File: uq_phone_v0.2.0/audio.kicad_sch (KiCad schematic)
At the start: 31 parts, among them J1 PJ-605, U13 TS3A5018RSVR, U14 NAU88C22YG, U9 AZV5001RA4-7

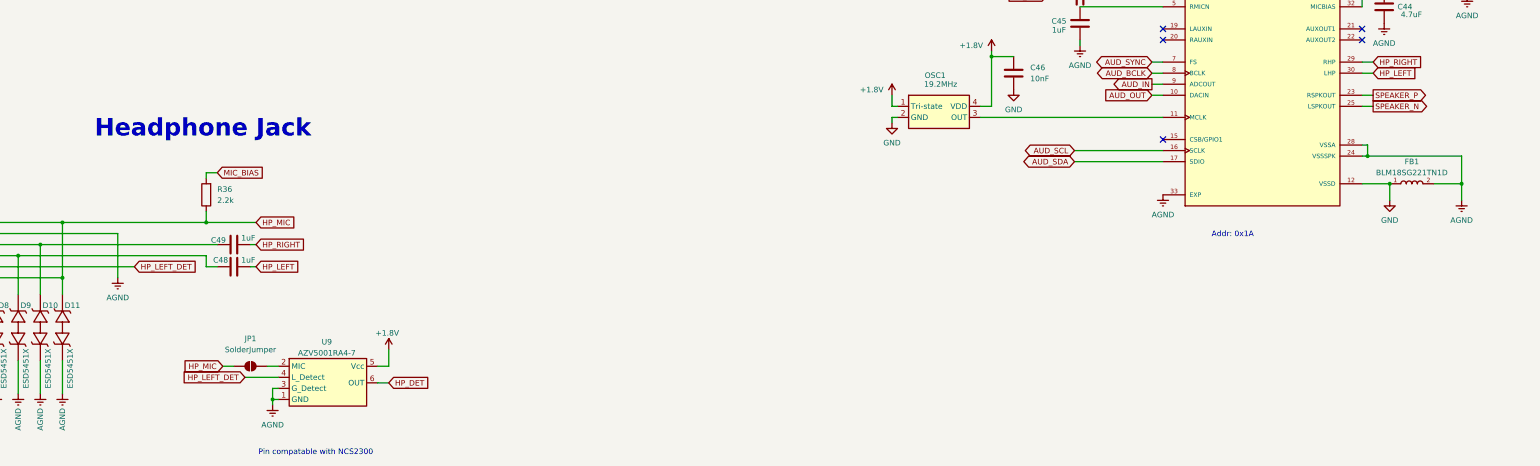
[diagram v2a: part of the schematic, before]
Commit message: Fixed display pinout
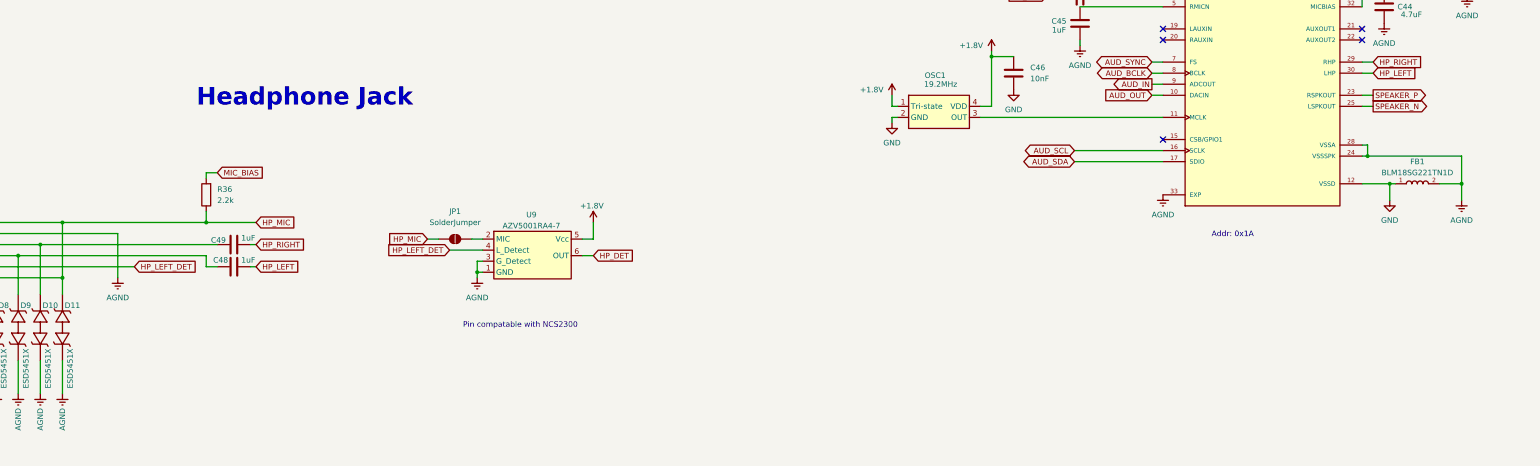
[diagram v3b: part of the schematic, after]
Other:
- moved on the sheet: FB1, JP1, U9
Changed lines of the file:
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@@
 	(text "Pin compatable with NCS2300"
 		(exclude_from_sim no)
-		(at 112.776 271.272 0)
+		(at 159.766 242.062 0)
 		(effects
 			(font
@@
 	(text "Headphone Jack"
 		(exclude_from_sim no)
-		(at 86.868 196.85 0)
+		(at 110.236 189.738 0)
 		(effects
 			(font
@@
 	)
 	(junction
-		(at 102.87 259.08)
+		(at 149.86 229.87)
 		(diameter 0)
 		(color 0 0 0 0)
@@
 	(wire
 		(pts
-			(xy 91.44 251.46) (xy 93.98 251.46)
+			(xy 138.43 222.25) (xy 140.97 222.25)
 		)
 		(stroke
@@
 	(wire
 		(pts
-			(xy 102.87 256.54) (xy 102.87 259.08)
+			(xy 149.86 227.33) (xy 149.86 229.87)
 		)
 		(stroke
@@
 	(wire
 		(pts
-			(xy 102.87 259.08) (xy 104.14 259.08)
+			(xy 149.86 229.87) (xy 151.13 229.87)
 		)
 		(stroke
@@
 	(wire
 		(pts
-			(xy 375.92 209.55) (xy 369.57 209.55)
+			(xy 375.92 209.55) (xy 370.84 209.55)
 		)
 		(stroke
@@
 	(wire
 		(pts
-			(xy 96.52 254) (xy 104.14 254)
+			(xy 143.51 224.79) (xy 151.13 224.79)
 		)
 		(stroke
@@
 	(wire
 		(pts
-			(xy 101.6 251.46) (xy 104.14 251.46)
+			(xy 148.59 222.25) (xy 151.13 222.25)
 		)
 		(stroke
@@
 	(wire
 		(pts
+			(xy 360.68 209.55) (xy 359.41 209.55)
+		)
+		(stroke
+			(width 0)
+			(type default)
+		)
+	)
+	(wire
+		(pts
 			(xy 378.46 129.54) (xy 378.46 130.81)
 		)
@@
 	(wire
 		(pts
-			(xy 129.54 251.46) (xy 127 251.46)
+			(xy 176.53 222.25) (xy 173.99 222.25)
 		)
 		(stroke
@@
 	(wire
 		(pts
-			(xy 102.87 260.35) (xy 102.87 259.08)
+			(xy 149.86 231.14) (xy 149.86 229.87)
 		)
 		(stroke
@@
 	(wire
 		(pts
-			(xy 129.54 247.65) (xy 129.54 251.46)
+			(xy 176.53 218.44) (xy 176.53 222.25)
 		)
 		(stroke
@@
 	(wire
 		(pts
-			(xy 129.54 255.27) (xy 127 255.27)
+			(xy 176.53 226.06) (xy 173.99 226.06)
 		)
 		(stroke
@@
 	(wire
 		(pts
-			(xy 104.14 256.54) (xy 102.87 256.54)
+			(xy 151.13 227.33) (xy 149.86 227.33)
 		)
 		(stroke
@@
 	(global_label "HP_DET"
 		(shape input)
-		(at 129.54 255.27 0)
+		(at 176.53 226.06 0)
 		(fields_autoplaced yes)
 		(effects
@@
 		)
 		(property "Intersheetrefs" "${INTERSHEET_REFS}"
-			(at 139.4799 255.27 0)
+			(at 186.4699 226.06 0)
 			(effects
 				(font
@@
 	(global_label "HP_LEFT_DET"
 		(shape input)
-		(at 96.52 254 180)
+		(at 143.51 224.79 180)
 		(fields_autoplaced yes)
 		(effects
@@
 		)
 		(property "Intersheetrefs" "${INTERSHEET_REFS}"
-			(at 81.3792 254 0)
+			(at 128.3692 224.79 0)
 			(effects
 				(font
@@
 	(global_label "HP_MIC"
 		(shape input)
-		(at 91.44 251.46 180)
+		(at 138.43 222.25 180)
 		(fields_autoplaced yes)
 		(effects
@@
 		)
 		(property "Intersheetrefs" "${INTERSHEET_REFS}"
-			(at 81.5605 251.46 0)
+			(at 128.5505 222.25 0)
 			(effects
 				(font
@@
 	(symbol
 		(lib_id "Misc:AZV5001")
-		(at 104.14 254 0)
+		(at 151.13 224.79 0)
 		(unit 1)
 		(exclude_from_sim no)
@@
 		(dnp no)
 		(property "Reference" "U9"
-			(at 115.316 245.872 0)
+			(at 162.306 216.662 0)
 			(effects
 				(font
@@
 		)
 		(property "Value" "AZV5001RA4-7"
-			(at 115.316 248.412 0)
+			(at 162.306 219.202 0)
 			(effects
 				(font
@@
 		)
 		(property "Footprint" "custom_footprints:DFN1210P6X_L1.2-W1.0-P0.40-BL"
-			(at 102.87 237.998 0)
+			(at 149.86 208.788 0)
 			(effects
 				(font
@@
 		)
 		(property "Datasheet" "https://www.lcsc.com/product-detail/C5246088.html?s_z=n_AZV5001"
-			(at 102.87 237.998 0)
+			(at 149.86 208.788 0)
 			(effects
 				(font
@@
 		)
 		(property "Description" "Low-Power Headset Detection IC in Miniaturized Package"
-			(at 102.87 237.998 0)
+			(at 149.86 208.788 0)
 			(effects
 				(font
@@
 		)
 		(property "LCSC PN" "C5246088"
-			(at 102.87 237.998 0)
+			(at 149.86 208.788 0)
 			(effects
 				(font
@@
 		)
 		(property "DESCRIPTION" ""
-			(at 104.14 254 0)
+			(at 151.13 224.79 0)
 			(effects
 				(font
@@
 		)
 		(property "LSCS PN" ""
-			(at 104.14 254 0)
+			(at 151.13 224.79 0)
 			(effects
 				(font
@@
 	(symbol
 		(lib_id "power:GNDREF")
-		(at 102.87 260.35 0)
+		(at 149.86 231.14 0)
 		(unit 1)
 		(exclude_from_sim no)
@@
 		(dnp no)
 		(property "Reference" "#PWR017"
-			(at 102.87 266.7 0)
+			(at 149.86 237.49 0)
 			(effects
 				(font
@@
 		)
 		(property "Value" "AGND"
-			(at 102.87 264.922 0)
+			(at 149.86 235.712 0)
 			(effects
 				(font
@@
 		)
 		(property "Footprint" ""
-			(at 102.87 260.35 0)
+			(at 149.86 231.14 0)
 			(effects
 				(font
@@
 		)
 		(property "Datasheet" ""
-			(at 102.87 260.35 0)
+			(at 149.86 231.14 0)
 			(effects
 				(font
@@
 		)
 		(property "Description" "Power symbol creates a global label with name \"GNDREF\" , reference supply ground"
-			(at 102.87 260.35 0)
+			(at 149.86 231.14 0)
 			(effects
 				(font
@@
 	(symbol
 		(lib_id "Jumper:SolderJumper_2_Open")
-		(at 97.79 251.46 0)
+		(at 144.78 222.25 0)
 		(unit 1)
 		(exclude_from_sim no)
@@
 		(fields_autoplaced yes)
 		(property "Reference" "JP1"
-			(at 97.79 245.11 0)
+			(at 144.78 215.9 0)
 			(effects
 				(font
@@
 		)
 		(property "Value" "SolderJumper"
-			(at 97.79 247.65 0)
+			(at 144.78 218.44 0)
 			(effects
 				(font
@@
 		)
 		(property "Footprint" "Jumper:SolderJumper-2_P1.3mm_Open_RoundedPad1.0x1.5mm"
-			(at 97.79 251.46 0)
+			(at 144.78 222.25 0)
 			(effects
 				(font
@@
 		)
 		(property "Datasheet" "~"
-			(at 97.79 251.46 0)
+			(at 144.78 222.25 0)
 			(effects
 				(font
@@
 		)
 		(property "Description" "Solder Jumper, 2-pole, open"
-			(at 97.79 251.46 0)
+			(at 144.78 222.25 0)
 			(effects
 				(font
@@
 		)
 		(property "DESCRIPTION" ""
-			(at 97.79 251.46 0)
+			(at 144.78 222.25 0)
 			(effects
 				(font
@@
 		)
 		(property "LSCS PN" ""
-			(at 97.79 251.46 0)
+			(at 144.78 222.25 0)
 			(effects
 				(font
@@
 	(symbol
 		(lib_id "power:+1V8")
-		(at 129.54 247.65 0)
+		(at 176.53 218.44 0)
 		(unit 1)
 		(exclude_from_sim no)
@@
 		(dnp no)
 		(property "Reference" "#PWR019"
-			(at 129.54 251.46 0)
+			(at 176.53 222.25 0)
 			(effects
 				(font
@@
 		)
 		(property "Value" "+1.8V"
-			(at 126.492 243.84 0)
+			(at 173.482 214.63 0)
 			(effects
 				(font
@@
 		)
 		(property "Footprint" ""
-			(at 129.54 247.65 0)
+			(at 176.53 218.44 0)
 			(effects
 				(font
@@
 		)
 		(property "Datasheet" ""
-			(at 129.54 247.65 0)
+			(at 176.53 218.44 0)
 			(effects
 				(font
@@
 		)
 		(property "Description" "Power symbol creates a global label with name \"+1V8\""
-			(at 129.54 247.65 0)
+			(at 176.53 218.44 0)
 			(effects
 				(font
@@
 	(symbol
 		(lib_id "BLM18SG221TN1D:BLM18SG221TN1D")
-		(at 359.41 209.55 0)
+		(at 360.68 209.55 0)
 		(unit 1)
 		(exclude_from_sim no)
@@
 		(fields_autoplaced yes)
 		(property "Reference" "FB1"
-			(at 364.49 204.47 0)
+			(at 365.76 204.47 0)
 			(effects
 				(font
@@
 		)
 		(property "Value" "BLM18SG221TN1D"
-			(at 364.49 207.01 0)
+			(at 365.76 207.01 0)
 			(effects
 				(font
@@
 		)
 		(property "Footprint" "BLM18SG221TN1D:BEADC1608X65N"
-			(at 359.41 200.66 0)
+			(at 360.68 200.66 0)
 			(effects
 				(font
@@
 		)
 		(property "Datasheet" ""
-			(at 359.41 209.55 0)
+			(at 360.68 209.55 0)
 			(effects
 				(font
@@
 		)
 		(property "Description" ""
-			(at 359.41 209.55 0)
+			(at 360.68 209.55 0)
 			(effects
 				(font
@@
 		)
 		(property "DigiKey_Part_Number" "490-5225-2-ND"
-			(at 359.41 200.66 0)
+			(at 360.68 200.66 0)
 			(effects
 				(font
@@
 		)
 		(property "SnapEDA_Link" "https://www.snapeda.com/parts/BLM18SG221TN1D/Murata/view-part/?ref=snap"
-			(at 359.41 200.66 0)
+			(at 360.68 200.66 0)
 			(effects
 				(font
@@
 		)
 		(property "Description_1" "220 Ohms @ 100 MHz 1 Power Line Ferrite Bead 0603 (1608 Metric) 2.5A 40mOhm"
-			(at 359.41 200.66 0)
+			(at 360.68 200.66 0)
 			(effects
 				(font
@@
 		)
 		(property "MF" "Murata Electronics"
-			(at 359.41 200.66 0)
+			(at 360.68 200.66 0)
 			(effects
 				(font
@@
 		)
 		(property "Package" "1608 Murata"
-			(at 359.41 200.66 0)
+			(at 360.68 200.66 0)
 			(effects
 				(font
@@
 		)
 		(property "Check_prices" "https://www.snapeda.com/parts/BLM18SG221TN1D/Murata/view-part/?ref=eda"
-			(at 359.41 200.66 0)
+			(at 360.68 200.66 0)
 			(effects
 				(font
@@
 		)
 		(property "MP" "BLM18SG221TN1D"
-			(at 359.41 200.66 0)
+			(at 360.68 200.66 0)
 			(effects
 				(font
@@
 		)
 		(property "LCSC PN" "C88988"
-			(at 359.41 200.66 0)
+			(at 360.68 200.66 0)
 			(effects
 				(font
@@
 		)
 		(property "DESCRIPTION" ""
-			(at 359.41 209.55 0)
+			(at 360.68 209.55 0)
 			(effects
 				(font
@@
 		)
 		(property "LSCS PN" ""
-			(at 359.41 209.55 0)
+			(at 360.68 209.55 0)
 			(effects
 				(font

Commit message: Routing improvements
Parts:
- J1: value PJ-605 -> PJ-605-6A
- OSC1: value 19.2MHz -> OT7EL89CJI-111YLC-19.2M
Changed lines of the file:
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@@
 	(text "Suitable for 8-Ohm 1W"
 		(exclude_from_sim no)
-		(at 77.724 146.812 0)
+		(at 383.54 190.5 0)
 		(effects
 			(font
@@
 	(text "Pin compatable with NCS2300"
 		(exclude_from_sim no)
-		(at 159.766 242.062 0)
+		(at 161.798 242.57 0)
 		(effects
 			(font
@@
 			)
 		)
-		(property "Value" "PJ-605"
+		(property "Value" "PJ-605-6A"
 			(at 26.162 215.9 0)
 			(effects
@@
 		(dnp no)
 		(property "Reference" "OSC1"
-			(at 255.016 184.658 0)
+			(at 251.46 202.438 0)
 			(effects
 				(font
@@
 			)
 		)
-		(property "Value" "19.2MHz"
-			(at 256.286 186.69 0)
+		(property "Value" "OT7EL89CJI-111YLC-19.2M"
+			(at 252.73 204.47 0)
 			(effects
 				(font

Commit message: Cleaning up adn fixing massive mistake
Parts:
- SP1: now fitted
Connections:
- net HP_MIC: now also C47.1, U14.4 (RMICP); no longer C47.2, D11.2, J1.5, J1.6, JP1.1 (A), R36.1
- net HP_MIC_GND: now reaches C45.1, U14.5 (RMICN)
- new net MIC_PIN: C47.2, D11.2, J1.5, J1.6, JP1.1 (A), R36.1
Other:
- note added: "8Ω 0.25W <1W, Ensure low volume"
- note added: "I2C Addr: 0x1A"
- note added: "UQ Phone"
- note removed: "Addr: 0x1A"
- note removed: "Audio Switch"
- note removed: "Codec"
- note removed: "Headphone Jack"
- note removed: "MIC"
- note removed: "Speaker"
- title: UQ Phone -> Audio System
- moved on the sheet: C36, C37, C38, C39, C40, C41, C42, C43, C44, C45, C46, C47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
